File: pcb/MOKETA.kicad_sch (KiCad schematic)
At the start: 88 parts, among them SW43 Reset, U1 Pro_Micro

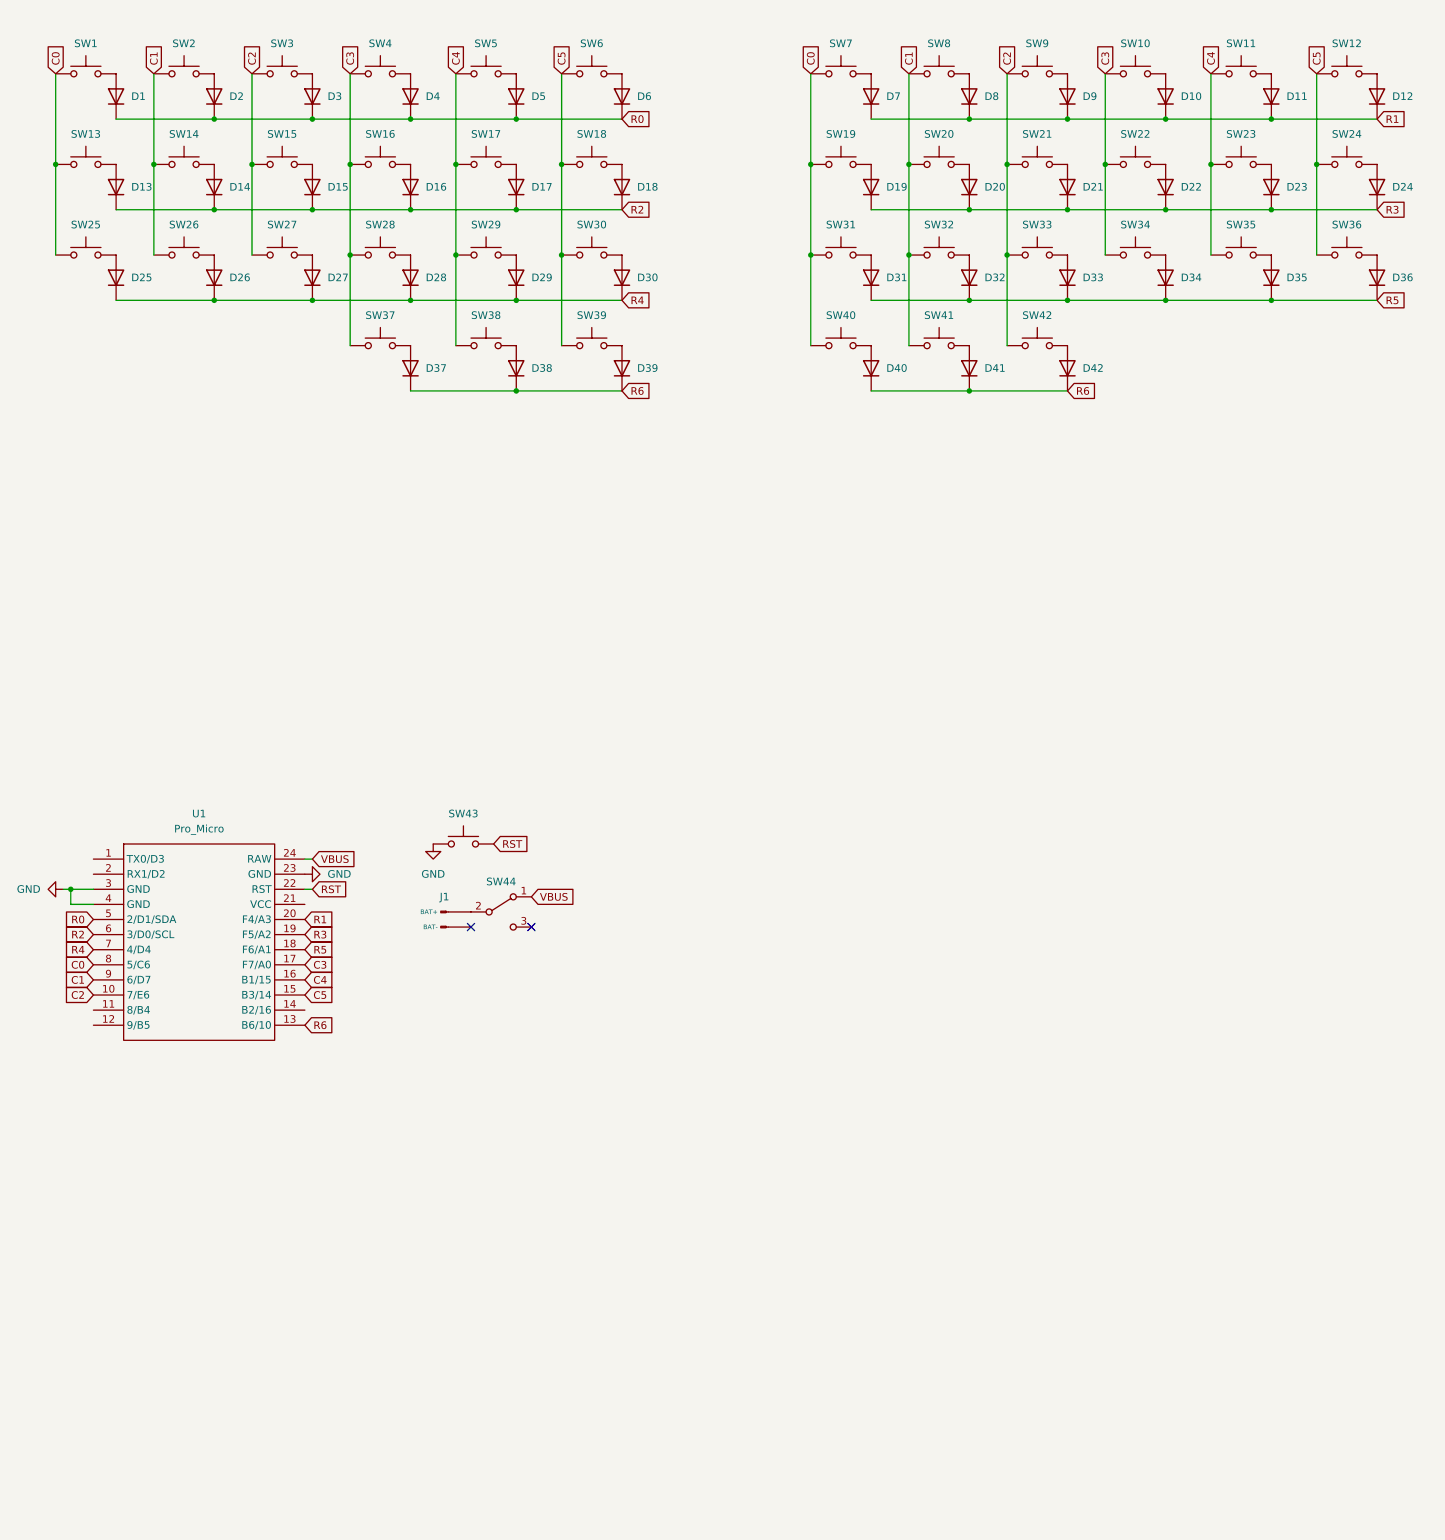
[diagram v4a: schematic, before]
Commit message: add RGB to scheme
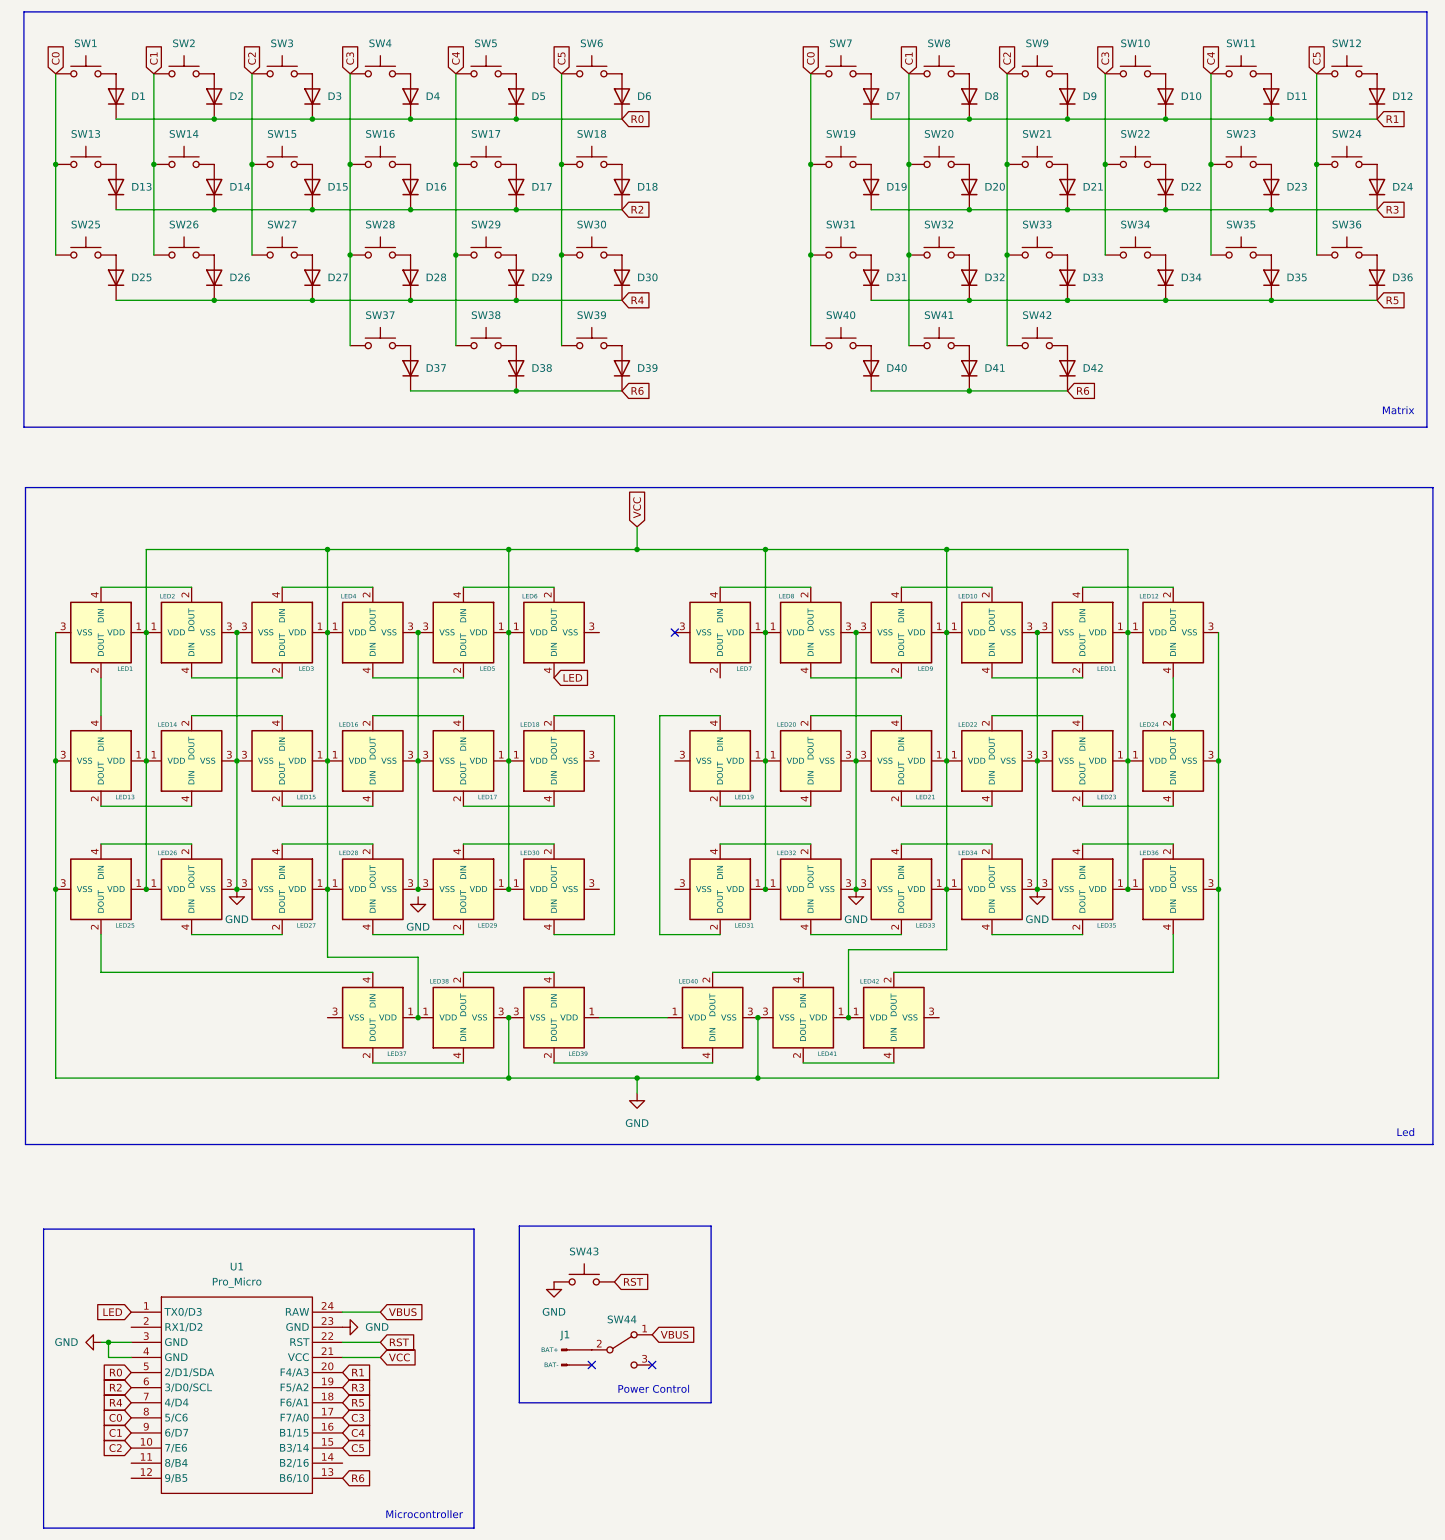
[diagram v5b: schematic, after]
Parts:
- added LED1, LED10, LED11, LED12, LED13, LED14, LED15, LED16, LED17, LED18, LED19, LED2, LED20, LED21, LED22, LED23, LED24, LED25, LED26, LED27, LED28, LED29, LED3, LED30, LED31, LED32, LED33, LED34, LED35, LED36, LED37, LED38, LED39, LED4, LED40, LED41, LED42, LED5, LED6, LED7, LED8, LED9: ~, symbol moketa:YS-SK6812MINI-E
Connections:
- net GND: now also LED1.3 (VSS), LED10.3 (VSS), LED11.3 (VSS), LED12.3 (VSS), LED13.3 (VSS), LED14.3 (VSS), LED15.3 (VSS), LED2.3 (VSS), LED20.3 (VSS), LED21.3 (VSS), LED22.3 (VSS), LED23.3 (VSS), LED24.3 (VSS), LED25.3 (VSS), LED26.3 (VSS), LED27.3 (VSS), LED3.3 (VSS), LED32.3 (VSS), LED33.3 (VSS), LED34.3 (VSS), LED35.3 (VSS), LED36.3 (VSS), LED38.3 (VSS), LED39.3 (VSS), LED40.3 (VSS), LED41.3 (VSS), LED8.3 (VSS), LED9.3 (VSS)
- net LED: now reaches U1.1 (TX0/D3)
- net LED: now also LED6.4 (DIN)
- net VCC: now reaches U1.21 (VCC)
- net VCC: now also LED1.1 (VDD), LED10.1 (VDD), LED11.1 (VDD), LED12.1 (VDD), LED13.1 (VDD), LED14.1 (VDD), LED15.1 (VDD), LED16.1 (VDD), LED17.1 (VDD), LED18.1 (VDD), LED19.1 (VDD), LED2.1 (VDD), LED20.1 (VDD), LED21.1 (VDD), LED22.1 (VDD), LED23.1 (VDD), LED24.1 (VDD), LED25.1 (VDD), LED26.1 (VDD), LED27.1 (VDD), LED28.1 (VDD), LED29.1 (VDD), LED3.1 (VDD), LED30.1 (VDD), LED31.1 (VDD), LED32.1 (VDD), LED33.1 (VDD), LED34.1 (VDD), LED35.1 (VDD), LED36.1 (VDD), LED37.1 (VDD), LED38.1 (VDD), LED4.1 (VDD), LED41.1 (VDD), LED42.1 (VDD), LED5.1 (VDD), LED6.1 (VDD), LED7.1 (VDD), LED8.1 (VDD), LED9.1 (VDD)
- new net: LED41.2 (DOUT), LED42.4 (DIN)
- new net: LED40.2 (DOUT), LED41.4 (DIN)
- new net: LED39.1 (VDD), LED40.1 (VDD)
- new net: LED39.2 (DOUT), LED40.4 (DIN)
- new net: LED5.4 (DIN), LED6.2 (DOUT)
- new net: LED8.4 (DIN), LED9.2 (DOUT)
- new net: LED10.2 (DOUT), LED9.4 (DIN)
- new net: LED25.2 (DOUT), LED37.4 (DIN)
- new net: LED25.4 (DIN), LED26.2 (DOUT)
- new net: LED21.2 (DOUT), LED22.4 (DIN)
- new net: LED20.2 (DOUT), LED21.4 (DIN)
- new net: LED14.2 (DOUT), LED15.4 (DIN)
- new net: LED13.2 (DOUT), LED14.4 (DIN)
- new net: LED4.4 (DIN), LED5.2 (DOUT)
- new net: LED16.3 (VSS), LED17.3 (VSS), LED28.3 (VSS), LED29.3 (VSS), LED4.3 (VSS), LED5.3 (VSS)
- new net: LED1.2 (DOUT), LED13.4 (DIN)
- new net: LED36.4 (DIN), LED42.2 (DOUT)
- new net: LED19.2 (DOUT), LED20.4 (DIN)
- new net: LED2.4 (DIN), LED3.2 (DOUT)
- new net: LED3.4 (DIN), LED4.2 (DOUT)
- new net: LED31.4 (DIN), LED32.2 (DOUT)
- new net: LED32.4 (DIN), LED33.2 (DOUT)
- new net: LED33.4 (DIN), LED34.2 (DOUT)
- new net: LED34.4 (DIN), LED35.2 (DOUT)
- new net: LED26.4 (DIN), LED27.2 (DOUT)
- new net: LED19.4 (DIN), LED31.2 (DOUT)
- new net: LED38.2 (DOUT), LED39.4 (DIN)
- new net: LED37.2 (DOUT), LED38.4 (DIN)
- new net: LED10.4 (DIN), LED11.2 (DOUT)
- new net: LED11.4 (DIN), LED12.2 (DOUT)
- new net: LED28.4 (DIN), LED29.2 (DOUT)
- new net: LED29.4 (DIN), LED30.2 (DOUT)
- new net: LED22.2 (DOUT), LED23.4 (DIN)
- new net: LED12.4 (DIN), LED24.2 (DOUT)
- new net: LED7.4 (DIN), LED8.2 (DOUT)
- new net: LED1.4 (DIN), LED2.2 (DOUT)
- new net: LED17.2 (DOUT), LED18.4 (DIN)
- new net: LED16.2 (DOUT), LED17.4 (DIN)
- new net: LED23.2 (DOUT), LED24.4 (DIN)
- new net: LED35.4 (DIN), LED36.2 (DOUT)
- new net: LED15.2 (DOUT), LED16.4 (DIN)
- new net: LED18.2 (DOUT), LED30.4 (DIN)
- new net: LED27.4 (DIN), LED28.2 (DOUT)
- no-connect marks 2 -> 3
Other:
- note added: "Led"
- note added: "Matrix"
- note added: "Microcontroller"
- note added: "Power Control"
- moved on the sheet: J1, SW43, SW44, U1

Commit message: some fix
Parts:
- J1: footprint (none) -> moketa:J_BATTERY
- LED1, LED10, LED11, LED12, LED13, LED14, LED15, LED16, LED17, LED18, LED19, LED2, LED20, LED21, LED22, LED23, LED24, LED25, LED26, LED27, LED28, LED29, LED3, LED30, LED31, LED32, LED33, LED34, LED35, LED36, LED37, LED38, LED39, LED4, LED40, LED41, LED42, LED5, LED6, LED7, LED8, LED9: footprint (none) -> moketa:YS-SK6812MINI-E
- SW43: footprint (none) -> moketa:SW_TACT
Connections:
- net GND: now also LED16.3 (VSS), LED17.3 (VSS), LED18.3 (VSS), LED19.3 (VSS), LED28.3 (VSS), LED29.3 (VSS), LED30.3 (VSS), LED31.3 (VSS), LED4.3 (VSS), LED5.3 (VSS), LED6.3 (VSS), LED7.3 (VSS)

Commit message: fix led
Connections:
- net GND: now also LED37.3 (VSS), LED42.3 (VSS)
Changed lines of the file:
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@@
+	)
+	(junction
+		(at 71.12 194.31)
+		(diameter 0)
+		(color 0 0 0 0)
 	)
 	(junction
@@
 	(junction
 		(at 52.07 63.5)
+		(diameter 0)
+		(color 0 0 0 0)
+	)
+	(junction
+		(at 173.99 194.31)
 		(diameter 0)
 		(color 0 0 0 0)
@@
 	(wire
 		(pts
+			(xy 173.99 184.15) (xy 173.99 194.31)
+		)
+		(stroke
+			(width 0)
+			(type default)
+		)
+	)
+	(wire
+		(pts
 			(xy 213.36 133.35) (xy 213.36 135.89)
 		)
@@
 	(wire
 		(pts
-			(xy 25.4 194.31) (xy 101.6 194.31)
+			(xy 25.4 194.31) (xy 71.12 194.31)
 		)
 		(stroke
@@
 	(wire
 		(pts
+			(xy 173.99 194.31) (xy 220.98 194.31)
+		)
+		(stroke
+			(width 0)
+			(type default)
+		)
+	)
+	(wire
+		(pts
 			(xy 198.12 154.94) (xy 213.36 154.94)
 		)
@@
 	(wire
 		(pts
-			(xy 143.51 194.31) (xy 220.98 194.31)
+			(xy 143.51 194.31) (xy 173.99 194.31)
 		)
 		(stroke
@@
 	(wire
 		(pts
+			(xy 71.12 194.31) (xy 101.6 194.31)
+		)
+		(stroke
+			(width 0)
+			(type default)
+		)
+	)
+	(wire
+		(pts
 			(xy 201.93 40.64) (xy 201.93 55.88)
 		)
@@
 		)
 		(stroke
+			(width 0)
+			(type default)
+		)
+	)
+	(wire
+		(pts
+			(xy 71.12 184.15) (xy 71.12 194.31)
+		)
+		(stroke

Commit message: add outline
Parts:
- SW44: footprint (none) -> moketa:BSI-10H
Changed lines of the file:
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@@
 			)
 		)
-		(property "Footprint" ""
+		(property "Footprint" "moketa:BSI-10H"
 			(at 123.444 249.174 0)
 			(effects
